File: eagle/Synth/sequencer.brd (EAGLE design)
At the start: 46.7 x 73.7 mm, 22 parts, among them U1 ATMEGA328P_PDIP, Y1 16MHz

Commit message: new stuff
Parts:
- removed U$1: (no value), cjk:RABID.AUDIO2
- added IC1: LM555N, adafruit:DIL08-ROUND
- added T1, T2: 2N2222, adafruit:TO92-EBC-OVAL
- moved POWER 7.73 mm to (40.6, 67.3), turned to 180 degrees
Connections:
- new net N$2: T1.B, T2.B
- new net V+: IC1.8
- net GND: now also IC1.1, T1.E, T2.E
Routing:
- net GND: track 63.8 -> 116.6 mm
- net VCC: track 152.7 -> 154.0 mm
- removed copper zone on layer 16, net GND
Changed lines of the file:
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@@
 <element name="U1" library="SparkFun-DigitalIC" package="DIL28-3" value="ATMEGA328P_PDIP" x="22.86" y="43.18"/>
 <element name="Y1" library="SparkFun-FreqCtrl" package="HC49US" value="16MHz" x="24.13" y="29.21" rot="R90"/>
-<element name="POWER" library="SparkFun-Connectors" package="1X04" value="" x="33.02" y="66.04"/>
+<element name="POWER" library="SparkFun-Connectors" package="1X04" value="" x="40.64" y="67.31" rot="R180"/>
 <element name="SIGNAL" library="SparkFun-Connectors" package="1X04" value="" x="7.62" y="68.58"/>
 <element name="D1" library="SparkFun-LED" package="LED3MM-NS" value="" x="22.86" y="53.34" rot="R90"/>
@@
 <element name="C2" library="SparkFun-Capacitors" package="1206" value="22pF" x="16.51" y="26.67" rot="R180"/>
 <element name="C3" library="SparkFun-Capacitors" package="1206" value="22pF" x="16.51" y="30.48" rot="R180"/>
-<element name="U$1" library="cjk" package="RABID.AUDIO2" value="" x="5.08" y="12.7" rot="MR90"/>
 <element name="S1" library="switch" package="TL3XYO" value="TRIGGER_MODE" x="35.56" y="21.59" rot="R90"/>
 <element name="S2" library="switch" package="TL3XYO" value="REVERSE" x="10.16" y="21.59" rot="R90"/>
+<element name="IC1" library="adafruit" package="DIL08-ROUND" value="LM555N" x="7.62" y="-5.08"/>
+<element name="T1" library="adafruit" package="TO92-EBC-OVAL" value="2N2222" x="3.81" y="-13.97"/>
+<element name="T2" library="adafruit" package="TO92-EBC-OVAL" value="2N2222" x="3.81" y="-22.86"/>
 </elements>
 <signals>
@@
 <contactref element="C3" pad="2"/>
 <contactref element="C2" pad="2"/>
-<polygon width="0.4064" layer="16">
-<vertex x="0" y="73.66"/>
-<vertex x="46.99" y="73.66"/>
-<vertex x="46.99" y="0"/>
-<vertex x="0" y="0"/>
-</polygon>
 <wire x1="21.46" y1="59.69" x2="12.7" y2="59.69" width="0.508" layer="1"/>
 <wire x1="12.7" y1="59.69" x2="11.43" y2="58.42" width="0.508" layer="1"/>
-<wire x1="24.26" y1="71.12" x2="33.02" y2="71.12" width="0.4064" layer="1"/>
-<wire x1="33.02" y1="71.12" x2="38.1" y2="66.04" width="0.4064" layer="1"/>
 <wire x1="17.91" y1="34.29" x2="19.05" y2="34.29" width="0.4064" layer="1"/>
 <wire x1="19.05" y1="34.29" x2="24.13" y2="39.37" width="0.4064" layer="1"/>
@@
 <wire x1="15.24" y1="25.4" x2="15.24" y2="26.54" width="0.4064" layer="1"/>
 <wire x1="15.24" y1="26.54" x2="15.11" y2="26.67" width="0.4064" layer="1"/>
+<wire x1="21.59" y1="46.99" x2="21.59" y2="44.45" width="0.4064" layer="1"/>
+<wire x1="21.59" y1="44.45" x2="24.13" y2="41.91" width="0.4064" layer="1"/>
+<wire x1="24.13" y1="41.91" x2="24.13" y2="39.37" width="0.4064" layer="1"/>
+<wire x1="35.56" y1="53.34" x2="35.56" y2="54.61" width="0.4064" layer="16"/>
+<wire x1="35.56" y1="54.61" x2="38.1" y2="57.15" width="0.4064" layer="16"/>
+<wire x1="38.1" y1="57.15" x2="38.1" y2="62.23" width="0.4064" layer="16"/>
+<wire x1="38.1" y1="62.23" x2="35.56" y2="64.77" width="0.4064" layer="16"/>
+<wire x1="35.56" y1="64.77" x2="35.56" y2="67.31" width="0.4064" layer="16"/>
+<wire x1="21.59" y1="46.99" x2="27.94" y2="53.34" width="0.4064" layer="16"/>
+<wire x1="27.94" y1="53.34" x2="35.56" y2="53.34" width="0.4064" layer="16"/>
+<wire x1="21.46" y1="59.69" x2="21.46" y2="57.02" width="0.4064" layer="1"/>
+<wire x1="21.46" y1="57.02" x2="20.32" y2="55.88" width="0.4064" layer="1"/>
+<wire x1="20.32" y1="55.88" x2="20.32" y2="49.53" width="0.4064" layer="1"/>
+<wire x1="20.32" y1="49.53" x2="21.59" y2="48.26" width="0.4064" layer="1"/>
+<wire x1="21.59" y1="48.26" x2="21.59" y2="46.99" width="0.4064" layer="1"/>
+<wire x1="24.26" y1="71.12" x2="33.02" y2="71.12" width="0.4064" layer="1"/>
+<wire x1="33.02" y1="71.12" x2="35.56" y2="68.58" width="0.4064" layer="1"/>
+<wire x1="35.56" y1="68.58" x2="35.56" y2="67.31" width="0.4064" layer="1"/>
+<contactref element="IC1" pad="1"/>
+<contactref element="T2" pad="E"/>
+<contactref element="T1" pad="E"/>
+<wire x1="3.81" y1="-8.89" x2="22.73" y2="17.78" width="0" layer="19" extent="1-1"/>
+<wire x1="1.27" y1="-15.24" x2="3.81" y2="-8.89" width="0" layer="19" extent="1-1"/>
+<wire x1="1.27" y1="-24.13" x2="1.27" y2="-15.24" width="0" layer="19" extent="1-1"/>
 </signal>
 <signal name="DIRECT_IN">
@@
 <contactref element="U1" pad="20"/>
 <contactref element="POWER" pad="2"/>
-<wire x1="26.67" y1="46.99" x2="26.67" y2="44.45" width="0.508" layer="16"/>
-<wire x1="26.67" y1="44.45" x2="21.59" y2="39.37" width="0.508" layer="16"/>
 <wire x1="21.59" y1="39.37" x2="21.59" y2="40.64" width="0.508" layer="16"/>
 <wire x1="21.59" y1="40.64" x2="20.32" y2="41.91" width="0.508" layer="16"/>
 <wire x1="20.32" y1="41.91" x2="8.89" y2="41.91" width="0.508" layer="16"/>
 <wire x1="8.89" y1="41.91" x2="6.35" y2="39.37" width="0.508" layer="16"/>
-<wire x1="41.91" y1="58.42" x2="41.91" y2="44.45" width="0.508" layer="16"/>
-<wire x1="41.91" y1="44.45" x2="26.67" y2="44.45" width="0.508" layer="16"/>
 <contactref element="RECORD" pad="1"/>
 <wire x1="11.43" y1="53.34" x2="7.62" y2="53.34" width="0.508" layer="16"/>
@@
 <wire x1="3.81" y1="49.53" x2="3.81" y2="41.91" width="0.508" layer="16"/>
 <wire x1="3.81" y1="41.91" x2="6.35" y2="39.37" width="0.508" layer="16"/>
-<wire x1="35.56" y1="64.77" x2="35.56" y2="66.04" width="0.508" layer="16"/>
-<wire x1="35.56" y1="64.77" x2="41.91" y2="58.42" width="0.508" layer="16"/>
 <wire x1="16.51" y1="16.51" x2="16.51" y2="13.6906" width="0.4064" layer="1"/>
 <wire x1="16.51" y1="13.6906" x2="16.2306" y2="13.4112" width="0.4064" layer="1"/>
@@
 <wire x1="33.02" y1="17.78" x2="34.29" y2="19.05" width="0.4064" layer="1"/>
 <wire x1="34.29" y1="19.05" x2="35.56" y2="19.05" width="0.4064" layer="1"/>
+<wire x1="38.1" y1="67.31" x2="38.1" y2="66.04" width="0.4064" layer="16"/>
+<wire x1="38.1" y1="66.04" x2="43.18" y2="60.96" width="0.4064" layer="16"/>
+<wire x1="43.18" y1="60.96" x2="43.18" y2="48.26" width="0.4064" layer="16"/>
+<wire x1="43.18" y1="48.26" x2="38.1" y2="43.18" width="0.4064" layer="16"/>
+<wire x1="38.1" y1="43.18" x2="30.48" y2="43.18" width="0.4064" layer="16"/>
+<wire x1="30.48" y1="43.18" x2="26.67" y2="46.99" width="0.4064" layer="16"/>
+<wire x1="21.59" y1="40.64" x2="22.86" y2="40.64" width="0.4064" layer="16"/>
+<wire x1="22.86" y1="40.64" x2="26.67" y2="44.45" width="0.4064" layer="16"/>
+<wire x1="26.67" y1="44.45" x2="26.67" y2="46.99" width="0.4064" layer="16"/>
 </signal>
 <signal name="TRIGGER">
@@
 <wire x1="8.89" y1="21.59" x2="6.35" y2="24.13" width="0.4064" layer="1"/>
 </signal>
+<signal name="V+">
+<contactref element="IC1" pad="8"/>
+</signal>
+<signal name="N$2">
+<contactref element="T2" pad="B"/>
+<contactref element="T1" pad="B"/>
+<wire x1="3.81" y1="-15.24" x2="3.81" y2="-24.13" width="0" layer="19" extent="1-1"/>
+</signal>
 </signals>

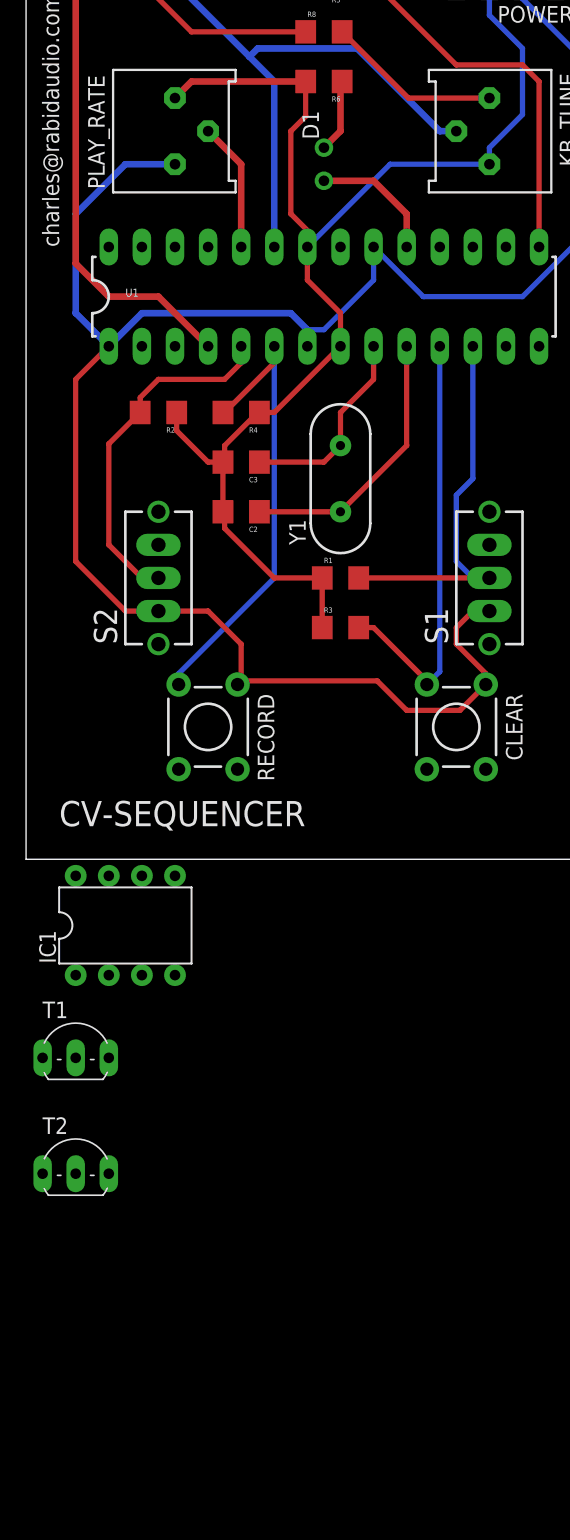
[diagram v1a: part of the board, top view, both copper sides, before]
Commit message: added ADC, cleaned up schematic
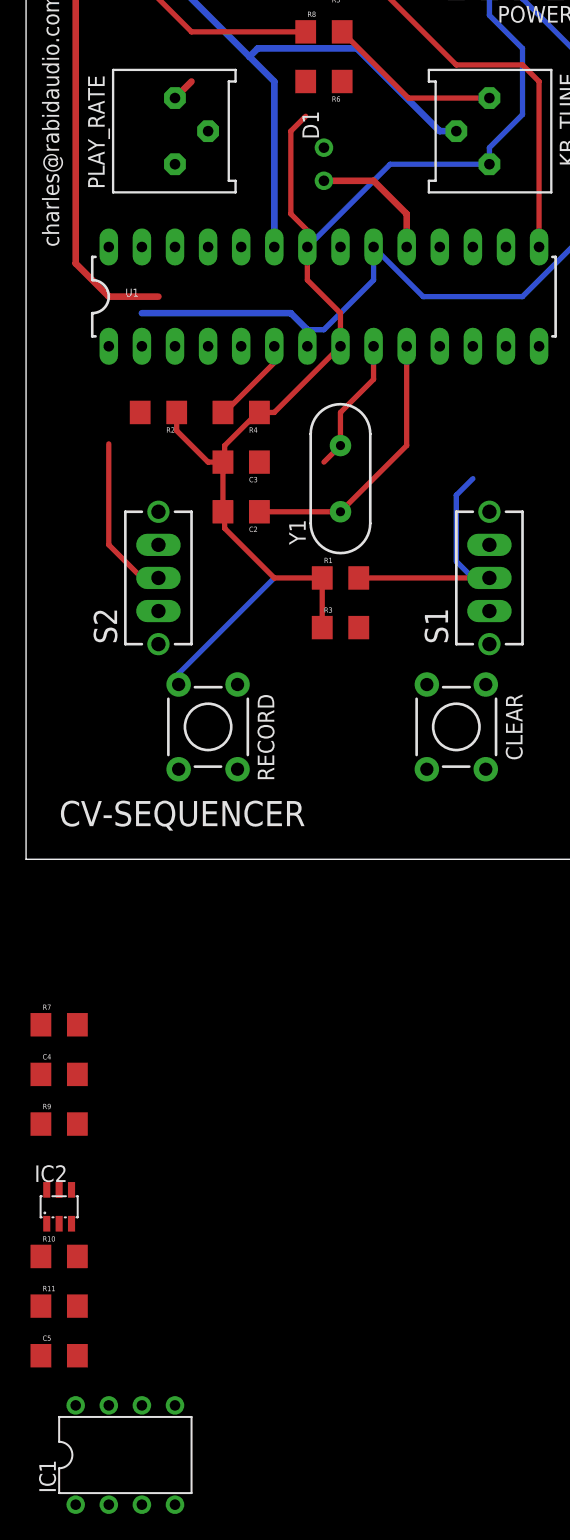
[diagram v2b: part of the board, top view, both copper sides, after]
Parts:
- removed T1, T2: 2N2222, adafruit:TO92-EBC-OVAL
- added C4: 100n, SparkFun-Capacitors:1206
- added C5: .1u, SparkFun-Capacitors:1206
- added IC2: (no value), ads11xx:SOT-23-6
- added R10, R11, R7, R9: 10k, SparkFun-Passives:1206
- IC1: value LM555N -> LM741P; device adafruit:DIL08-ROUND -> linear:DIL08
- moved IC1 40.6 mm to (7.62, -45.7)
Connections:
- new net N$10: U1.5
- new net N$12: R9.2, U1.4
- new net N$5: R7.1, U1.1
- new net N$9: U1.6
- new net SCL: IC2.3, R11.1, U1.28
- new net SDA: IC2.4, R10.1, U1.27
- new net V-: IC1.4
- net GND: now also C4.2, C5.2, IC2.2, IC2.6; no longer IC1.1, T1.E, T2.E
- net N$2: now also U1.12; no longer T1.B, T2.B
- net RECORD: no longer U1.6
- net REVERSE: no longer U1.5
- net TRIGGER: now also R9.1; no longer U1.4
- net TRIGGERMODE: no longer U1.12
- net V+: now also IC1.7; no longer IC1.8
- net VCC: now also C4.1, C5.1, CLEAR.2, IC2.5, R10.2, R11.2, R7.2; no longer CLEAR.1, U1.1
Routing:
- net VCC: track 154.0 -> 65.0 mm
- net CLEAR: track 33.6 -> 0.00 mm
- net RECORD: track 35.8 -> 16.7 mm
- net REVERSE: track 27.3 -> 12.6 mm
- net GND: track 116.6 -> 105.1 mm
- net TRIGGERMODE: track 30.1 -> 20.0 mm
- net RATE: track 9.94 -> 0.00 mm
- net N$3: track 5.66 -> 0.00 mm
- net TRIGGER: track 47.4 -> 42.0 mm
- net N$6: track 15.4 -> 10.5 mm

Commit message: uncommited board changes
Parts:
- added C6: 1u, SparkFun-Capacitors:1206
- added C7: 10UF-25V-10%(SMT-TANT), SparkFun-Capacitors:EIA6032-NOM
- added R12, R13, R14, R15, R16: 100k, SparkFun-Passives:1206
- added R17: 680\, SparkFun-Passives:1206
- added RATE: 100K, SparkFun-Electromechanical:ALPS_POT_KIT
- added U2: MAX5217GUA+, cjk:21-0036K
- moved C4 110.0 mm to (67.3, 72.4), turned to 180 degrees
- moved C5 110.0 mm to (67.3, 50.8), turned to 180 degrees
- moved R10 110.0 mm to (67.3, 58.4)
- moved R11 110.0 mm to (67.3, 54.6)
- moved R7 110.0 mm to (67.3, 76.2)
- moved R9 110.0 mm to (67.3, 68.6)
- moved IC2 109.1 mm to (50.8, 71.1), turned to 90 degrees
- moved IC1 94.3 mm to (74.9, 20.3), turned to 270 degrees
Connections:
- removed net V+: IC1.7
- new net N$13: IC1.3, R12.1, R13.1, R14.2
- new net N$15: R17.2, RATE.P$3
- new net N$17: C6.2, C7.A, R15.1, R16.2
- new net N$18: C6.1, IC1.2, R17.1
- new net N$19: IC1.6, R12.2, RATE.P$1, RATE.P$2
- net GND: now also C7.C, R14.1, R16.1, U2.2, U2.5, U2.8
- net SCL: now also U2.3
- net SDA: now also U2.4
- net VCC: now also IC1.7, R13.2, R15.2, U2.1, U2.7
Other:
- board size 46.7 x 73.7 mm -> 86 x 106.7 mm

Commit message: updated sequencer eagle files for current version
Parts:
- removed PLAY_RATE: 10k, bourns:3386P
- removed SIGNAL: (no value), SparkFun-Connectors:1X04
- added IO: HEADER-06X1-FEMALE, GeekAmmo:06X1-PTH
- added R18, R20: 10k, SparkFun-Passives:1206
- added R19: 220???, SparkFun-Passives:1206
- added S3: RATE_SRC, switch:TL3XYO
- moved R7 64.3 mm to (16.5, 36.8), turned to 270 degrees
- moved R16 56.8 mm to (16.5, 30.5)
- moved R9 53.2 mm to (26.7, 34.3), turned to 90 degrees
- moved R11 52.1 mm to (15.2, 54.6), turned to 90 degrees
- moved R13 49.7 mm to (25.4, 16.5)
- moved R10 48.4 mm to (19.1, 54.6), turned to 90 degrees
- moved C6 45.5 mm to (25.4, 30.5)
- moved U2 44.9 mm to (7.62, 67.3)
- moved IC2 44.7 mm to (7.62, 59.7)
- moved R14 44.2 mm to (25.4, 22.9)
- moved R17 43.1 mm to (25.4, 26.7)
- moved IC1 42.1 mm to (33.0, 24.1)
- moved C7 41.2 mm to (25.4, 34.3), turned to 180 degrees
- moved R12 34.9 mm to (40.6, 15.2)
- moved POWER 33.0 mm to (10.2, 80.0)
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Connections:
- removed net N$10: U1.5
- removed net N$12: R9.2, U1.4
- removed net N$19: IC1.6, R12.2, RATE.P$1, RATE.P$2
- removed net N$9: U1.6
- new net PLAYBACKGATE: IO.1, R20.2, U1.14
- new net RATE_EXTERNAL: IO.2, S3.3
- new net RATE_INTERNAL: IC1.6, R12.2, RATE.P$1, RATE.P$2, S3.1
- net CLEAR: now also U1.12; no longer U1.11
- net CV_OUT: now also IO.6; no longer SIGNAL.4
- net DIRECT_IN: now also IO.4; no longer SIGNAL.2
- net GND: now also R18.1, R19.1, R20.1, R9.1; no longer KB_TUNE.3, PLAY_RATE.3
- net KEYBOARD_CV_IN: now also IO.5; no longer SIGNAL.1
- net N$2: now also KB_TUNE.3, R19.2; no longer U1.12
- net RATE: now also R18.2, S3.2, U1.4; no longer PLAY_RATE.2, U1.24
- net RECORD: now also U1.11
- net REVERSE: now also U1.6
- net TRIGGER: now also IO.3, R9.2, U1.5; no longer R9.1, SIGNAL.3
- net TRIGGERMODE: now also U1.13
- net VCC: no longer PLAY_RATE.1
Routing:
- net GND: track 105.1 -> 0.00 mm
- net VCC: track 65.0 -> 0.00 mm
- net TRIGGER: track 42.0 -> 0.00 mm
- net PLAYBACKGATE: track 0.00 -> 40.7 mm
- net N$1: track 31.0 -> 0.00 mm
- net DIRECT_IN: track 44.0 -> 20.1 mm
- net N$7: track 21.0 -> 0.00 mm
- net TRIGGERMODE: track 20.0 -> 0.00 mm
- net RECORD: track 16.7 -> 0.00 mm
- net N$4: track 13.4 -> 0.00 mm
- net REVERSE: track 12.6 -> 0.00 mm
- net N$3: track 0.00 -> 10.9 mm
- net N$6: track 10.5 -> 0.00 mm
- net N$8: track 9.94 -> 18.8 mm
- net CV_OUT: track 10.6 -> 18.0 mm
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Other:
- board size 86 x 106.7 mm -> 68.2 x 82.5 mm

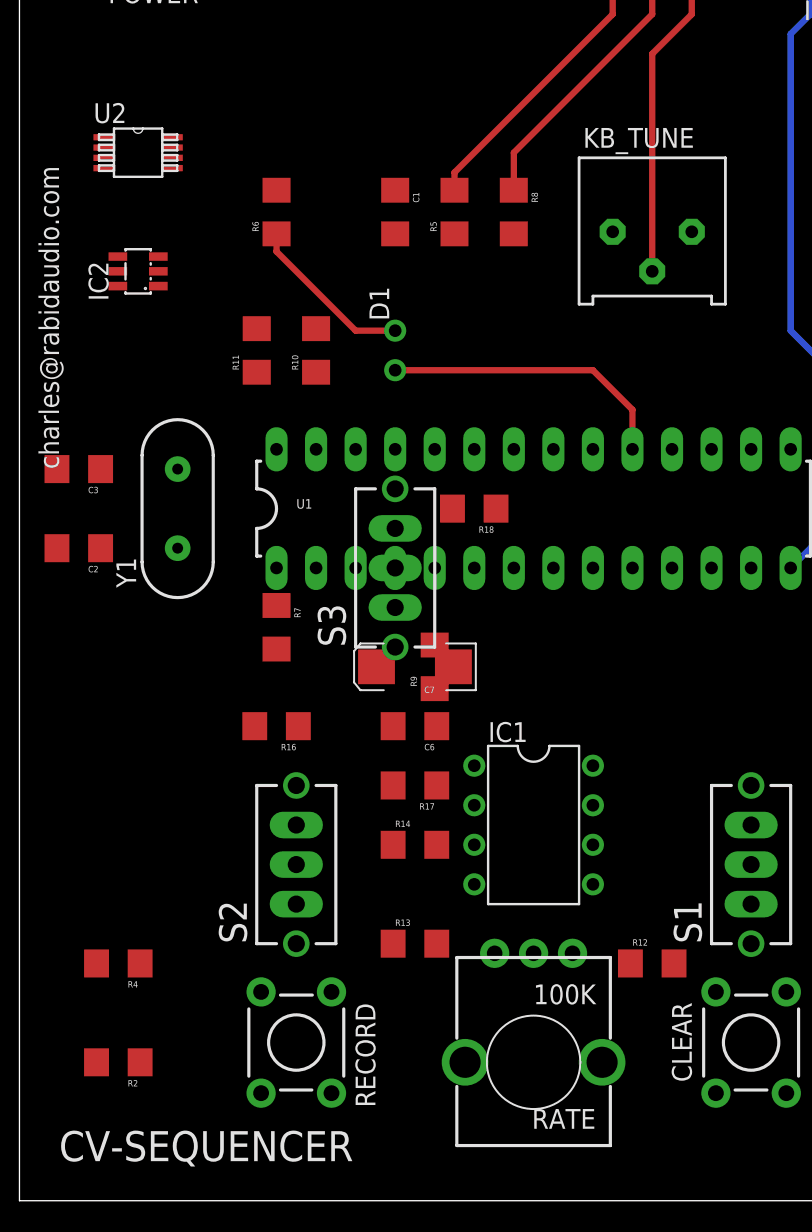
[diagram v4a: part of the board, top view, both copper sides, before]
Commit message: updated schematic for BOM
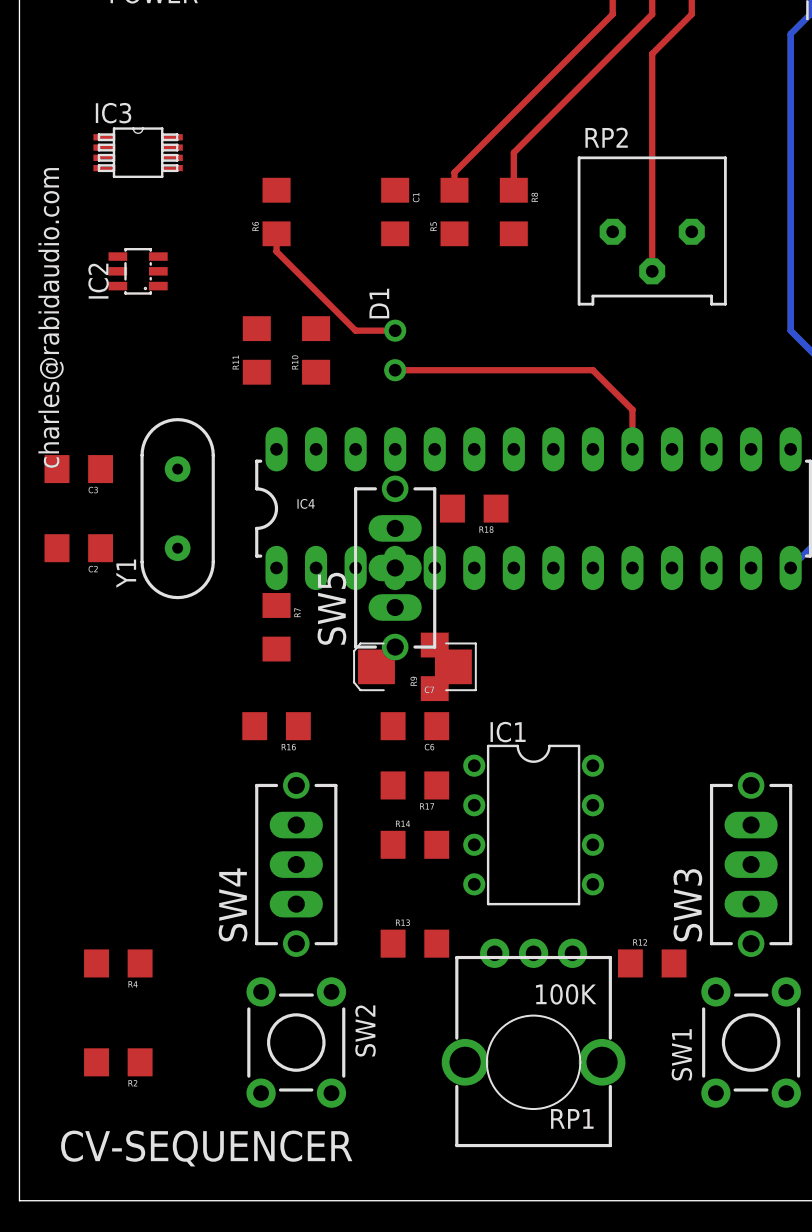
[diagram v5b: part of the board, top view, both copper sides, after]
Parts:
- R17: value 680\ -> 680
- R19: value 220??? -> 2.2K
- SW3: value TRIGGER_MODE -> (none)
- SW4: value REVERSE -> (none)
- renumbered CLEAR to SW1, KB_TUNE to RP2, RATE to RP1, RECORD to SW2, S1 to SW3, S2 to SW4, S3 to SW5, U1 to IC4, U2 to IC3
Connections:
- new net SW3: SW3.1
- net VCC: no longer SW3.1

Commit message: board tweaks
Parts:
- C4: value 100n -> .1u
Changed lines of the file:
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@@
 <element name="SW4" library="switch" package="TL3XYO" value="" x="17.78" y="21.59" rot="R90"/>
 <element name="R7" library="SparkFun-Passives" package="1206" value="10k" x="16.51" y="36.83" rot="R270"/>
-<element name="C4" library="SparkFun-Capacitors" package="1206" value="100n" x="55.88" y="44.45"/>
+<element name="C4" library="SparkFun-Capacitors" package="1206" value=".1u" x="55.88" y="44.45"/>
 <element name="R9" library="SparkFun-Passives" package="1206" value="10k" x="26.67" y="34.29" rot="R90"/>
 <element name="IC2" library="ads11xx" package="SOT-23-6" value="" x="7.62" y="59.69" rot="R90"/>

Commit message: added other files
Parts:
- removed R19: 2.2K, SparkFun-Passives:1206
- removed R8: 47k, SparkFun-Passives:1206
- added RP3: 10K, bourns:3386P
- IC3: value MAX5217GUA+ -> DAC8571; device cjk:21-0036K -> cjk:8MSOP
- moved R15 53.5 mm to (5.08, 30.5), turned to 180 degrees
- moved R7 49.6 mm to (66.0, 34.3), turned to 0 degrees
- moved R2 36.8 mm to (33.0, 34.3), turned to 90 degrees
- moved R4 35.9 mm to (36.8, 34.3), turned to 90 degrees
- moved R9 35.9 mm to (62.2, 29.2), turned to 180 degrees
- moved R12 30.2 mm to (11.4, 22.9)
- moved IC1 28.5 mm to (6.35, 14.0)
- moved R17 27.9 mm to (6.35, 6.35), turned to 0 degrees
- moved R18 23.7 mm to (52.1, 38.1)
- moved RP2 21.7 mm to (61.0, 69.8)
- moved R13 21.3 mm to (5.08, 22.9), turned to 180 degrees
- moved C6 20.7 mm to (5.08, 26.7), turned to 0 degrees
- moved C7 20.4 mm to (5.08, 35.6)
- moved R3 18.3 mm to (40.6, 34.3), turned to 90 degrees
- moved SW2 16.1 mm to (33.0, 5.08), turned to 180 degrees
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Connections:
- removed net KEYBOARD_CV_IN: IO.5, R8.1
- removed net N$4: R8.2, RP2.1
- removed net SW3: SW3.1
- new net CV_IN: IO.5, RP2.1
- net CLEAR: now also SW1.4
- net CV_OUT: now also RP3.2
- net DIRECT_IN: now also IC2.1; no longer IC4.23, IO.4
- net GND: now also RP2.3, RP3.3; no longer IC3.2, R19.1
- net N$2: now also IC3.3, IC3.4, RP3.1; no longer R19.2, RP2.3
- net RECORD: now also IO.4, SW2.4
- net SCL: now also IC3.6; no longer IC3.3
- net SDA: now also IC3.7; no longer IC3.4
- net VCC: now also IC3.2, SW1.1, SW2.2, SW3.1; no longer IC3.7
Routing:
- net VCC: track 0.00 -> 110.6 mm
- net RECORD: track 0.00 -> 49.8 mm
- net CLEAR: track 0.00 -> 47.8 mm
- net PLAYBACKGATE: track 40.7 -> 0.00 mm
- net GND: track 0.00 -> 36.9 mm
- net RATE_EXTERNAL: track 0.00 -> 35.2 mm
- net RATE_INTERNAL: track 0.00 -> 30.5 mm
- net TRIGGERMODE: track 0.00 -> 24.5 mm
- net N$18: track 0.00 -> 23.5 mm
- net REVERSE: track 0.00 -> 22.7 mm
- net DIRECT_IN: track 20.1 -> 0.00 mm
- net N$13: track 0.00 -> 20.1 mm, vias 0 -> 1
- net N$8: track 18.8 -> 0.00 mm
- net CV_OUT: track 18.0 -> 0.00 mm
- net KEYBOARD_CV_IN: track 17.5 -> 0.00 mm
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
